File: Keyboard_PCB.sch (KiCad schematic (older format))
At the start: 24 parts, among them SW1 SW_Push, U1 ATmega32U4-AU, Y1 16MHz

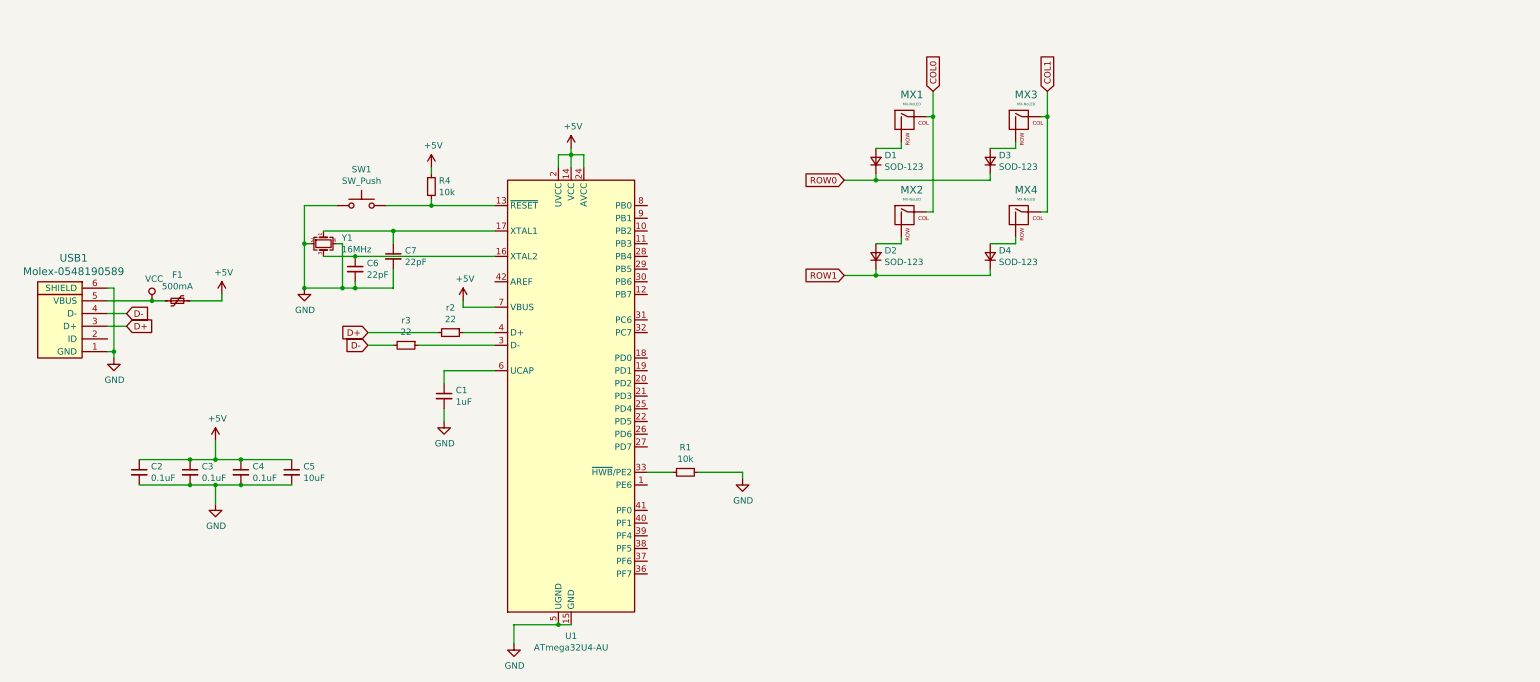
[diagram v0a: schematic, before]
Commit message: keyboard laid out in schematic
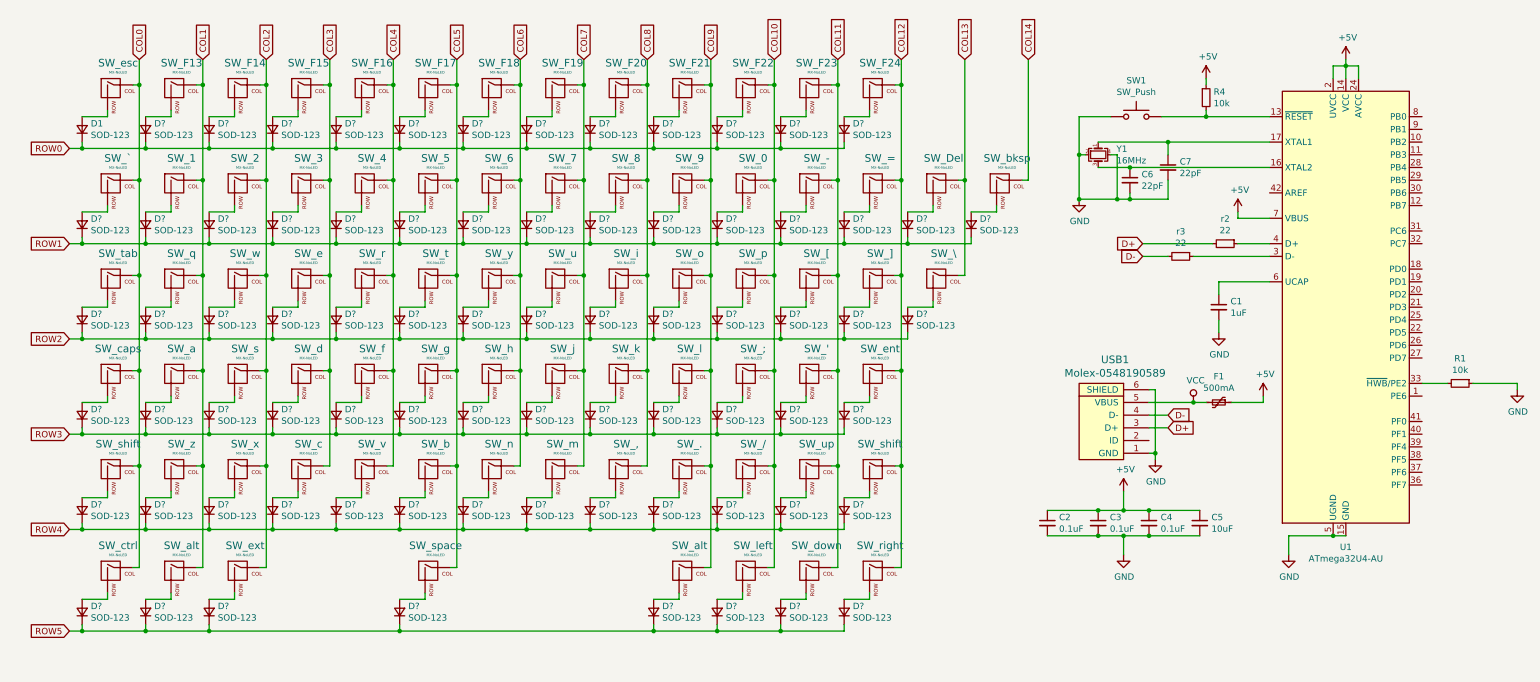
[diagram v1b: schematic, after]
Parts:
- added D? (x72): SOD-123, Diode_SMD:D_SOD-123, symbol Device:D_Small
- added SW_', SW_,, SW_-, SW_., SW_/, SW_0, SW_2, SW_3, SW_4, SW_5, SW_6, SW_7, SW_8, SW_9, SW_;, SW_=, SW_Del, SW_F14, SW_F15, SW_F16, SW_F17, SW_F18, SW_F19, SW_F20, SW_F21, SW_F22, SW_F23, SW_F24, SW_[, SW_], SW_a, SW_alt (x2), SW_b, SW_bksp, SW_c, SW_ctrl, SW_d, SW_down, SW_e, SW_ext, SW_f, SW_g, SW_h, SW_i, SW_j, SW_k, SW_l, SW_left, SW_m, SW_n, SW_o, SW_p, SW_q, SW_r, SW_right, SW_s, SW_shift (x2), SW_space, SW_t, SW_u, SW_up, SW_v, SW_w, SW_x, SW_y, SW_z: MX-NoLED, MX_Alps_Hybrid:MX-1U-NoLED, symbol MX_Alps_Hybrid:MX-NoLED
- added SW_\, SW_tab: MX-NoLED, MX_Alps_Hybrid:MX-1.5U-NoLED, symbol MX_Alps_Hybrid:MX-NoLED
- added SW_caps: MX-NoLED, MX_Alps_Hybrid:MX-1.75U-NoLED, symbol MX_Alps_Hybrid:MX-NoLED
- added SW_ent: MX-NoLED, MX_Alps_Hybrid:MX-2.25U-NoLED, symbol MX_Alps_Hybrid:MX-NoLED
- renumbered D3 to D?, D2 to D?, D4 to D?, MX4 to SW_1, MX3 to SW_F13, MX2 to SW_`, MX1 to SW_esc
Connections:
- net COL0: now also SW_caps.1 (COL), SW_ctrl.1 (COL), SW_shift.1 (COL), SW_tab.1 (COL)
- net COL1: now also SW_a.1 (COL), SW_alt.1 (COL), SW_q.1 (COL), SW_z.1 (COL)
- net ROW0: now also D?.1 (K), D?.1 (K), D?.1 (K), D?.1 (K), D?.1 (K), D?.1 (K), D?.1 (K), D?.1 (K), D?.1 (K), D?.1 (K), D?.1 (K)
- net ROW1: now also D?.1 (K), D?.1 (K), D?.1 (K), D?.1 (K), D?.1 (K), D?.1 (K), D?.1 (K), D?.1 (K), D?.1 (K), D?.1 (K), D?.1 (K), D?.1 (K), D?.1 (K)
- new net: D?.2 (A), SW_F14.2 (ROW)
- new net: D?.2 (A), SW_F15.2 (ROW)
- new net: D?.2 (A), SW_F16.2 (ROW)
- new net: D?.2 (A), SW_F17.2 (ROW)
- new net: D?.2 (A), SW_F18.2 (ROW)
- new net: D?.2 (A), SW_F19.2 (ROW)
- new net: D?.2 (A), SW_F20.2 (ROW)
- new net: D?.2 (A), SW_F21.2 (ROW)
- new net: D?.2 (A), SW_F22.2 (ROW)
- new net: D?.2 (A), SW_F23.2 (ROW)
- new net: D?.2 (A), SW_F24.2 (ROW)
- new net: D?.2 (A), SW_tab.2 (ROW)
- new net: D?.2 (A), SW_caps.2 (ROW)
- new net: D?.2 (A), SW_shift.2 (ROW) (x2)
- new net: D?.2 (A), SW_ctrl.2 (ROW)
- new net: D?.2 (A), SW_2.2 (ROW)
- new net: D?.2 (A), SW_3.2 (ROW)
- new net: D?.2 (A), SW_4.2 (ROW)
- new net: D?.2 (A), SW_5.2 (ROW)
- new net: D?.2 (A), SW_6.2 (ROW)
- new net: D?.2 (A), SW_7.2 (ROW)
- new net: D?.2 (A), SW_8.2 (ROW)
- new net: D?.2 (A), SW_9.2 (ROW)
- new net: D?.2 (A), SW_0.2 (ROW)
- new net: D?.2 (A), SW_-.2 (ROW)
- new net: D?.2 (A), SW_=.2 (ROW)
- new net: D?.2 (A), SW_Del.2 (ROW)
- new net: D?.2 (A), SW_w.2 (ROW)
- new net: D?.2 (A), SW_e.2 (ROW)
- new net: D?.2 (A), SW_r.2 (ROW)
- new net: D?.2 (A), SW_t.2 (ROW)
- new net: D?.2 (A), SW_y.2 (ROW)
- new net: D?.2 (A), SW_u.2 (ROW)
- new net: D?.2 (A), SW_i.2 (ROW)
- new net: D?.2 (A), SW_o.2 (ROW)
- new net: D?.2 (A), SW_p.2 (ROW)
- new net: D?.2 (A), SW_[.2 (ROW)
- new net: D?.2 (A), SW_].2 (ROW)
- new net: D?.2 (A), SW_\.2 (ROW)
- new net: D?.2 (A), SW_q.2 (ROW)
- new net: D?.2 (A), SW_s.2 (ROW)
- new net: D?.2 (A), SW_d.2 (ROW)
- new net: D?.2 (A), SW_f.2 (ROW)
- new net: D?.2 (A), SW_g.2 (ROW)
- new net: D?.2 (A), SW_h.2 (ROW)
- new net: D?.2 (A), SW_j.2 (ROW)
- new net: D?.2 (A), SW_k.2 (ROW)
- new net: D?.2 (A), SW_l.2 (ROW)
- new net: D?.2 (A), SW_;.2 (ROW)
- new net: D?.2 (A), SW_'.2 (ROW)
- new net: D?.2 (A), SW_ent.2 (ROW)
- new net: D?.2 (A), SW_a.2 (ROW)
- new net: D?.2 (A), SW_x.2 (ROW)
- new net: D?.2 (A), SW_c.2 (ROW)
- new net: D?.2 (A), SW_v.2 (ROW)
- new net: D?.2 (A), SW_b.2 (ROW)
- new net: D?.2 (A), SW_n.2 (ROW)
- new net: D?.2 (A), SW_m.2 (ROW)
- new net: D?.2 (A), SW_,.2 (ROW)
- new net: D?.2 (A), SW_..2 (ROW)
- new net: D?.2 (A), SW_/.2 (ROW)
- new net: D?.2 (A), SW_up.2 (ROW)
- new net: D?.2 (A), SW_z.2 (ROW)
- new net: D?.2 (A), SW_ext.2 (ROW)
- new net: D?.2 (A), SW_space.2 (ROW)
- new net: D?.2 (A), SW_alt.2 (ROW) (x2)
- new net: D?.2 (A), SW_left.2 (ROW)
- new net: D?.2 (A), SW_down.2 (ROW)
- new net: D?.2 (A), SW_right.2 (ROW)
- new net: D?.2 (A), SW_bksp.2 (ROW)
- new net COL10: SW_/.1 (COL), SW_0.1 (COL), SW_;.1 (COL), SW_F22.1 (COL), SW_left.1 (COL), SW_p.1 (COL)
- new net COL11: SW_'.1 (COL), SW_-.1 (COL), SW_F23.1 (COL), SW_[.1 (COL), SW_down.1 (COL), SW_up.1 (COL)
- new net COL12: SW_=.1 (COL), SW_F24.1 (COL), SW_].1 (COL), SW_ent.1 (COL), SW_right.1 (COL), SW_shift.1 (COL)
- new net COL13: SW_Del.1 (COL), SW_\.1 (COL)
- new net COL14: SW_bksp.1 (COL)
- new net COL2: SW_2.1 (COL), SW_F14.1 (COL), SW_ext.1 (COL), SW_s.1 (COL), SW_w.1 (COL), SW_x.1 (COL)
- new net COL3: SW_3.1 (COL), SW_F15.1 (COL), SW_c.1 (COL), SW_d.1 (COL), SW_e.1 (COL)
- new net COL4: SW_4.1 (COL), SW_F16.1 (COL), SW_f.1 (COL), SW_r.1 (COL), SW_v.1 (COL)
- new net COL5: SW_5.1 (COL), SW_F17.1 (COL), SW_b.1 (COL), SW_g.1 (COL), SW_space.1 (COL), SW_t.1 (COL)
- new net COL6: SW_6.1 (COL), SW_F18.1 (COL), SW_h.1 (COL), SW_n.1 (COL), SW_y.1 (COL)
- new net COL7: SW_7.1 (COL), SW_F19.1 (COL), SW_j.1 (COL), SW_m.1 (COL), SW_u.1 (COL)
- new net COL8: SW_,.1 (COL), SW_8.1 (COL), SW_F20.1 (COL), SW_i.1 (COL), SW_k.1 (COL)
- new net COL9: SW_..1 (COL), SW_9.1 (COL), SW_F21.1 (COL), SW_alt.1 (COL), SW_l.1 (COL), SW_o.1 (COL)
- new net ROW2: D?.1 (K), D?.1 (K), D?.1 (K), D?.1 (K), D?.1 (K), D?.1 (K), D?.1 (K), D?.1 (K), D?.1 (K), D?.1 (K), D?.1 (K), D?.1 (K), D?.1 (K), D?.1 (K)
- new net ROW3: D?.1 (K), D?.1 (K), D?.1 (K), D?.1 (K), D?.1 (K), D?.1 (K), D?.1 (K), D?.1 (K), D?.1 (K), D?.1 (K), D?.1 (K), D?.1 (K), D?.1 (K)
- new net ROW4: D?.1 (K), D?.1 (K), D?.1 (K), D?.1 (K), D?.1 (K), D?.1 (K), D?.1 (K), D?.1 (K), D?.1 (K), D?.1 (K), D?.1 (K), D?.1 (K), D?.1 (K)
- new net ROW5: D?.1 (K), D?.1 (K), D?.1 (K), D?.1 (K), D?.1 (K), D?.1 (K), D?.1 (K), D?.1 (K)
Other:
- moved on the sheet: C1, C2, C3, C4, C5, C6, C7, D1, D?, F1, R1, R4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

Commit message: updated PCB
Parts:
- SW_shift1: renamed from SW_shift; footprint MX_Alps_Hybrid:MX-1U-NoLED -> MX_Alps_Hybrid:MX-2.25U
- SW_shift2: renamed from SW_shift; footprint MX_Alps_Hybrid:MX-1U-NoLED -> MX_Alps_Hybrid:MX-1.75U
- SW_space1: renamed from SW_space; footprint MX_Alps_Hybrid:MX-1U-NoLED -> MX_Alps_Hybrid:MX-7U
- gave numbers to parts that had none: 75
- renumbered SW_' to SW_'1, SW_, to SW_,1, SW_- to SW_-1, SW_. to SW_.1, SW_/ to SW_/1, SW_; to SW_;1, SW_= to SW_=1, SW_Del to SW_Del1, SW_[ to SW_[1, SW_\ to SW_\1, SW_] to SW_]1, SW_` to SW_`1, SW_a to SW_a1, SW_alt to SW_alt1, SW_alt to SW_alt2, SW_b to SW_b1, SW_bksp to SW_bksp1, SW_c to SW_c1, SW_caps to SW_caps1, SW_ctrl to SW_ctrl1, SW_d to SW_d1, SW_down to SW_down1, SW_e to SW_e1, SW_ent to SW_ent1, SW_esc to SW_esc1, SW_ext to SW_ext1, SW_f to SW_f1, SW_g to SW_g1, SW_h to SW_h1, SW_i to SW_i1, SW_j to SW_j1, SW_k to SW_k1, SW_l to SW_l1, SW_left to SW_left1, SW_m to SW_m1, SW_n to SW_n1, SW_o to SW_o1, SW_p to SW_p1, SW_q to SW_q1, SW_r to SW_r1, SW_right to SW_right1, SW_s to SW_s1, SW_t to SW_t1, SW_tab to SW_tab1, SW_u to SW_u1, SW_up to SW_up1, SW_v to SW_v1, SW_w to SW_w1, SW_x to SW_x1, SW_y to SW_y1, SW_z to SW_z1

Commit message: added parts
added OLED, Slidepot, and Rotary encoder to sch and pcb
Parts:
- added OL1: OLED, kbd:OLED_v2, symbol kbd:OLED
- added R2: PSM60-081A-103B2, PSM60-081A-103B2:PSM60-081A-103B2, symbol PSM60-081A-103B2:PSM60-081A-103B2
- added S1: PEC11-4215F-S24, SW-Bournes:PEC11R-4xxx-Sxxxx, symbol SW-Bournes-Pro-Audio:PEC11-4215F-S24
- SW_shift1: footprint MX_Alps_Hybrid:MX-2.25U -> MX_Alps_Hybrid:MX-2.25U-NoLED
- SW_shift2: footprint MX_Alps_Hybrid:MX-1.75U -> MX_Alps_Hybrid:MX-1.75U-NoLED
- SW_space1: footprint MX_Alps_Hybrid:MX-7U -> MX_Alps_Hybrid:MX-7U-NoLED
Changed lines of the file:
@@
 F 0 "SW_shift1" H 1333 4473 60  0000 C CNN
 F 1 "MX-NoLED" H 1333 4399 20  0000 C CNN
-F 2 "MX_Alps_Hybrid:MX-2.25U" H 675 4225 60  0001 C CNN
+F 2 "MX_Alps_Hybrid:MX-2.25U-NoLED" H 675 4225 60  0001 C CNN
 F 3 "" H 675 4225 60  0001 C CNN
 	1    1300 4250
@@
 F 0 "SW_shift2" H 7333 4473 60  0000 C CNN
 F 1 "MX-NoLED" H 7333 4399 20  0000 C CNN
-F 2 "MX_Alps_Hybrid:MX-1.75U" H 6675 4225 60  0001 C CNN
+F 2 "MX_Alps_Hybrid:MX-1.75U-NoLED" H 6675 4225 60  0001 C CNN
 F 3 "" H 6675 4225 60  0001 C CNN
 	1    7300 4250
@@
 F 0 "SW_space1" H 3833 5273 60  0000 C CNN
 F 1 "MX-NoLED" H 3833 5199 20  0000 C CNN
-F 2 "MX_Alps_Hybrid:MX-7U" H 3175 5025 60  0001 C CNN
+F 2 "MX_Alps_Hybrid:MX-7U-NoLED" H 3175 5025 60  0001 C CNN
 F 3 "" H 3175 5025 60  0001 C CNN
 	1    3800 5050
@@
 	1    0    0    -1
 $EndComp
+$Comp
+L kbd:OLED OL1
+U 1 1 638FACB6
+P 15500 1200
+F 0 "OL1" H 16128 1269 51  0000 L CNN
+F 1 "OLED" H 16128 1179 47  0000 L CNN
+F 2 "kbd:OLED_v2" H 15500 1300 60  0001 C CNN
+F 3 "" H 15500 1300 60  0001 C CNN
+	1    15500 1200
+	1    0    0    -1
+$EndComp
+$Comp
+L SW-Bournes-Pro-Audio:PEC11-4215F-S24 S1
+U 1 1 638FEEB5
+P 15400 2500
+F 0 "S1" H 15375 2797 60  0000 C CNN
+F 1 "PEC11-4215F-S24" H 15375 2691 60  0000 C CNN
+F 2 "SW-Bournes:PEC11R-4xxx-Sxxxx" H 15300 2550 60  0001 C CNN
+F 3 "http://www.bourns.com/docs/Product-Datasheets/pec11R.pdf" H 15250 2850 60  0001 C CNN
+F 4 "0.00@0" H 15700 3150 60  0001 C CNN "Pricing"
+F 5 "Bournes Pro Audio" H 15400 2950 60  0001 C CNN "Manufacturer"
+F 6 "PEC11R Series - 12 mm Incremental Encoder" H 15400 3050 60  0001 C CNN "Description"
+	1    15400 2500
+	1    0    0    -1
+$EndComp
+$Comp
+L PSM60-081A-103B2:PSM60-081A-103B2 R2
+U 1 1 63910CA9
+P 14250 3750
+F 0 "R2" H 15050 4137 60  0000 C CNN
+F 1 "PSM60-081A-103B2" H 15050 4031 60  0000 C CNN
+F 2 "PSM60-081A-103B2:PSM60-081A-103B2" H 15050 3990 60  0001 C CNN
+F 3 "" H 14250 3750 60  0000 C CNN
+	1    14250 3750
+	1    0    0    -1
+$EndComp
